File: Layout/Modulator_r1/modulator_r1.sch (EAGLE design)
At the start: 3 parts, among them IC1 FT232RL, U1 ATMEGA328P-AU

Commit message: Progress on board.
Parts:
- added C1: 10nF, resistor:C-EUC0603
- added C2: 100nF, resistor:C-EUC0603
- added C3: 4u7, resistor:C-EUC0603
- added J$2: SMA_EDGE, SparkFun-Connectors:SMA_EDGE
- added JP1: AVR_SPI_PRG_6NS, SparkFun-Connectors:AVR_SPI_PRG_6NS
- added JP2: USB-B, SparkFun-Connectors:USBPTH
- added L1: FB, resistor:L-EU0207/12
- added LED1, LED2, LED3, LED4: (no value), led:LEDCHIPLED_1206
- added U$1: CC1125RHBT, Texas Instruments_By_element14_Batch_1:CC1125RHBT
- added U$6: MCP1700T-3302E/TT, Ava:MCP1700T-3302E/TT
- added U2: TPS79933QDDCRQ1, Texas Instruments_By_element14_Batch_1:TPS79933QDDCRQ1
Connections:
- new net +3V3: JP1.2, U$6.VOUT, U1.AVCC, U1.VCC, U1.VCC_2
- new net AVR_NRESET: JP1.5, U1.PC6
- new net GND: C1.2, C2.2, C3.2, IC1.GND, IC1.GND@1, IC1.GND@2, IC1.GND@A, J$1.GND@0, J$1.GND@1, J$1.GND@2, J$1.GND@3, J$2.GND@0, J$2.GND@1, J$2.GND@2, J$2.GND@3, JP1.6, L1.2, LED1.C, LED2.C, LED3.C, LED4.C, U$1.GND_PAD, U$6.GND, U1.GND, U1.GND_2, U1.GND_3, U2.GND
- new net MISO: JP1.1, U$1.MISO, U1.PB4
- new net MOSI: JP1.4, U$1.MOSI, U1.PB3
- new net N$1: IC1.USBDM, JP2.D-
- new net N$2: IC1.USBDP, JP2.D+
- new net N$3: JP2.GND, L1.1
- new net NSS: U$1.CSN, U1.PB2
- new net SCK: JP1.3, U$1.SCK, U1.PB5
- new net UART_RX: IC1.RXD, U1.PD1
- new net UART_TX: IC1.TXD, U1.PD0
- new net VCCIO: C1.1, C2.1, C3.1, IC1.VCC, IC1.VCCIO, JP2.VBUS, U$6.VIN, U2.IN

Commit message: Layout progress.
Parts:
- added C10: 1n8, resistor:C-EUC0402
- added C11, C12: 12p, resistor:C-EUC0402
- added C13, C14, C18: 5p1, resistor:C-EUC0402
- added C15: 56p, resistor:C-EUC0402
- added C16: 39p, resistor:C-EUC0402
- added C17: 2p2, resistor:C-EUC0402
- added C19: 6p2, resistor:C-EUC0402
- added C20, C21, C22, C23, C24, C25, C26, C28, C29, C8, C9: 47n, resistor:C-EUC0402
- added C27: 100p, resistor:C-EUC0402
- added C4: 100nF, resistor:C-EUC0603
- added C5: 10nF, resistor:C-EUC0603
- added C6: 220n, resistor:C-EUC0402
- added C7: 10n, resistor:C-EUC0402
- added L2: FB, resistor:L-EU0207/10
- added L3, L6: 56n, resistor:L-EUL0402
- added L4, L5: 27n, resistor:L-EUL0402
- added L7: 15n, resistor:L-EUL0402
- added L8: 43n, resistor:L-EUL0402
- added L9: 22n, resistor:L-EUL0402
- added Q1: FA-20H, crystal:FA-20H
- added R1: 56K, resistor:R-EU_R0402
- added R2: 18R, resistor:R-EU_R0402
- L1: device resistor:L-EU0207/12 -> resistor:L-EU0207/10
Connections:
- new net CC_IO0: U$1.GPIO0
- new net CC_IO2: U$1.GPIO2
- new net CC_IO3: U$1.GPIO3
- new net CC_LNA_N: C13.2, L3.1, L4.1, U$1.LNA_N
- new net CC_LNA_P: C14.1, L3.2, L5.1, U$1.LNA_P
- new net CC_NRESET: U$1.NRESET
- new net CC_RF_PA: C16.2, L6.2, U$1.PA
- new net CC_VDD: C15.1, C20.1, C21.1, C22.1, C23.1, C24.1, C25.1, C26.1, C27.1, C28.1, C29.1, R2.2, U$1.AVDD_IF, U$1.AVDD_PFD_CHP, U$1.AVDD_RF, U$1.AVDD_SYNTH2, U$1.AVDD_SYNTH_1, U$1.AVDD_XOSC, U$1.DVDD_1, U$1.DVDD_2, U$1.VDD_GUARD, U2.OUT
- new net N$10: C7.1, U$1.DCPL_VCO
- new net N$11: C6.1, U$1.DCPL
- new net N$12: C10.2, U$1.LPF1
- new net N$13: C10.1, U$1.LPF0
- new net N$14: C11.1, Q1.1, U$1.XOSC_Q2
- new net N$15: C19.1, L8.1, L9.2
- new net N$16: C12.1, Q1.3, U$1.XOSC_Q1
- new net N$17: C14.2, J$1.SIGNAL, L4.2
- new net N$18: C17.1, C18.1, L7.1, L8.2
- new net N$19: C16.1, C17.2, L7.2
- new net N$21: C15.2, L6.1, R2.1
- new net N$4: C5.1, JP2.VBUS, L2.1
- new net N$5: C4.1, IC1.3V3OUT
- new net N$6: J$2.SIGNAL, L9.1
- new net N$7: R1.1, U$1.RBIAS
- new net N$8: C9.1, U$1.DCPL_XOSC
- new net N$9: C8.1, U$1.DCPL_PFD_CHIP
- net GND: now also C11.2, C12.2, C13.1, C18.2, C19.2, C20.2, C21.2, C22.2, C23.2, C24.2, C25.2, C26.2, C27.2, C28.2, C29.2, C4.2, C5.2, C6.2, C7.2, C8.2, C9.2, IC1.TEST, L5.2, Q1.2, Q1.4, R1.2
- net VCCIO: now also L2.2; no longer JP2.VBUS
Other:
- moved on the sheet: JP2, L1

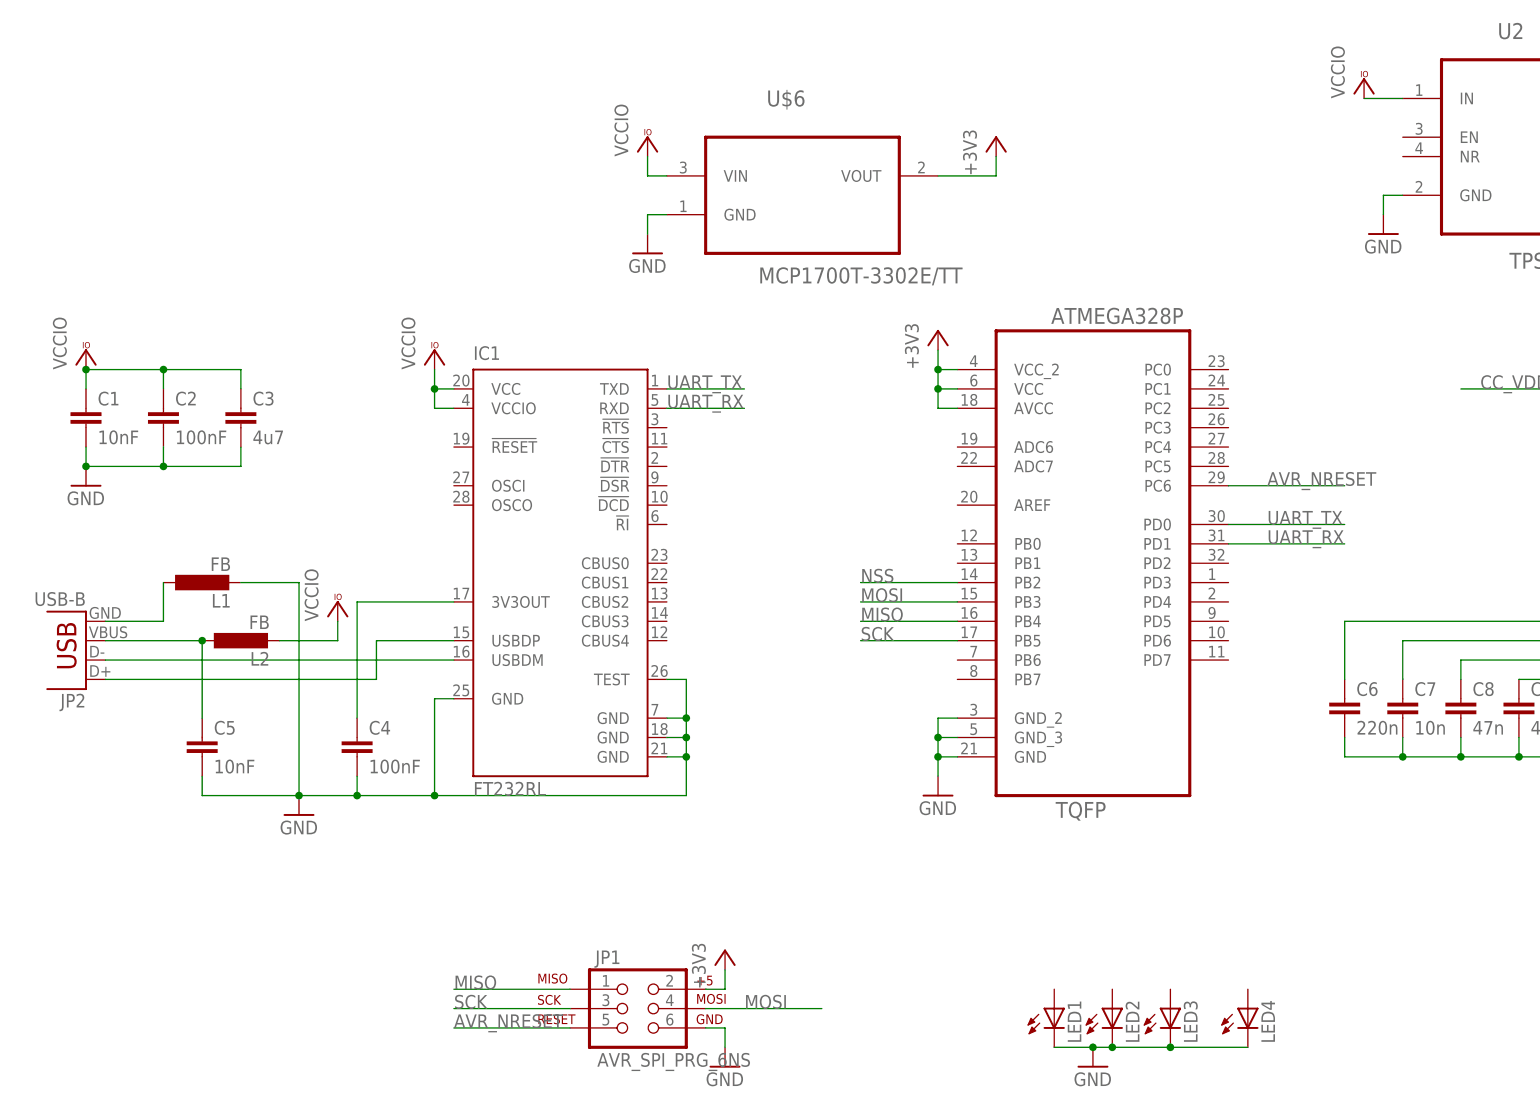
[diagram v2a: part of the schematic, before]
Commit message: Add USB power switch, start routing.
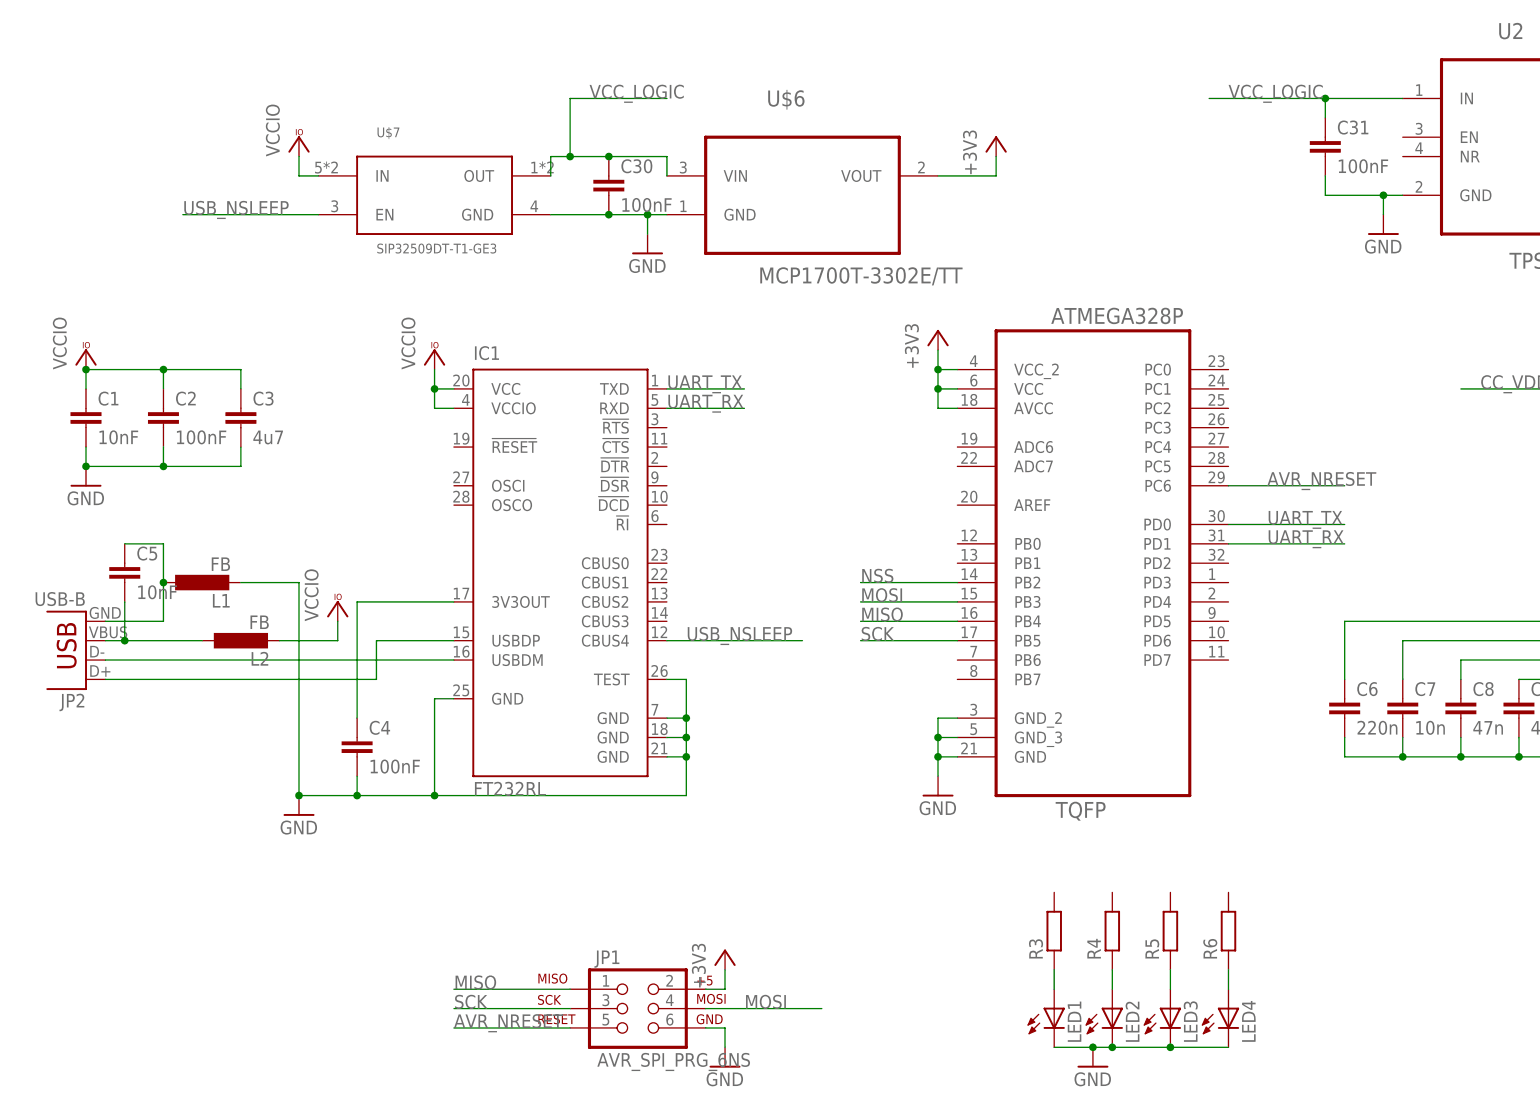
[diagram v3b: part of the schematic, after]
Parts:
- added C30, C31: 100nF, resistor:C-EUC0603
- added R3, R4, R5, R6: (no value), resistor:R-EU_R0603
- added U$7: SIP32509DT-T1-GE3, phil-ic:SIP32509DT-T1-GE3
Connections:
- new net N$22: LED1.A, R3.1
- new net N$23: LED2.A, R4.1
- new net N$24: LED3.A, R5.1
- new net N$25: LED4.A, R6.1
- new net USB_NSLEEP: IC1.CBUS4, U$7.EN
- new net VCC_LOGIC: C30.1, C31.1, U$6.VIN, U$7.OUT, U2.IN
- net GND: now also C30.2, C31.2, U$7.GND; no longer C5.2
- net N$3: now also C5.1
- net N$4: now also C5.2; no longer C5.1
- net VCCIO: now also U$7.IN; no longer U$6.VIN, U2.IN
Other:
- moved on the sheet: C5, LED4
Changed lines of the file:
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@@
 <part name="C2" library="resistor" deviceset="C-EU" device="C0603" value="100nF"/>
 <part name="C3" library="resistor" deviceset="C-EU" device="C0603" value="4u7"/>
-<part name="VCC3" library="supply1" deviceset="VCCIO" device=""/>
 <part name="GND5" library="supply1" deviceset="GND" device=""/>
 <part name="GND6" library="supply1" deviceset="GND" device=""/>
-<part name="VCC4" library="supply1" deviceset="VCCIO" device=""/>
 <part name="GND7" library="supply1" deviceset="GND" device=""/>
 <part name="+3V1" library="supply1" deviceset="+3V3" device=""/>
@@
 <part name="C28" library="resistor" deviceset="C-EU" device="C0402" value="47n"/>
 <part name="C29" library="resistor" deviceset="C-EU" device="C0402" value="47n"/>
+<part name="U$7" library="phil-ic" deviceset="SIP32509DT-T1-GE3" device=""/>
+<part name="VCC6" library="supply1" deviceset="VCCIO" device=""/>
+<part name="C30" library="resistor" deviceset="C-EU" device="C0603" value="100nF"/>
+<part name="R3" library="resistor" deviceset="R-EU_" device="R0603"/>
+<part name="R4" library="resistor" deviceset="R-EU_" device="R0603"/>
+<part name="R5" library="resistor" deviceset="R-EU_" device="R0603"/>
+<part name="R6" library="resistor" deviceset="R-EU_" device="R0603"/>
+<part name="C31" library="resistor" deviceset="C-EU" device="C0603" value="100nF"/>
 </parts>
 <sheets>
@@
 <instance part="LED2" gate="G$1" x="45.72" y="-22.86"/>
 <instance part="LED3" gate="G$1" x="53.34" y="-22.86"/>
-<instance part="LED4" gate="G$1" x="63.5" y="-22.86"/>
+<instance part="LED4" gate="G$1" x="60.96" y="-22.86"/>
 <instance part="U$6" gate="A" x="5.08" y="86.36"/>
 <instance part="L1" gate="G$1" x="-73.66" y="33.02" rot="R90"/>
@@
 <instance part="C2" gate="G$1" x="-78.74" y="55.88"/>
 <instance part="C3" gate="G$1" x="-68.58" y="55.88"/>
-<instance part="VCC3" gate="G$1" x="-15.24" y="91.44"/>
 <instance part="GND5" gate="1" x="-15.24" y="76.2"/>
 <instance part="GND6" gate="1" x="81.28" y="78.74"/>
-<instance part="VCC4" gate="G$1" x="78.74" y="99.06"/>
 <instance part="GND7" gate="1" x="-5.08" y="-30.48"/>
 <instance part="+3V1" gate="G$1" x="30.48" y="91.44"/>
@@
 <instance part="C4" gate="G$1" x="-53.34" y="12.7"/>
 <instance part="L2" gate="G$1" x="-68.58" y="25.4" rot="R90"/>
-<instance part="C5" gate="G$1" x="-73.66" y="12.7"/>
+<instance part="C5" gate="G$1" x="-83.82" y="35.56"/>
 <instance part="C6" gate="G$1" x="76.2" y="17.78"/>
 <instance part="C7" gate="G$1" x="83.82" y="17.78"/>
@@
 <instance part="C28" gate="G$1" x="175.26" y="93.98"/>
 <instance part="C29" gate="G$1" x="182.88" y="93.98"/>
+<instance part="U$7" gate="G$1" x="-43.18" y="83.82"/>
+<instance part="VCC6" gate="G$1" x="-60.96" y="91.44"/>
+<instance part="C30" gate="G$1" x="-20.32" y="86.36"/>
+<instance part="R3" gate="G$1" x="38.1" y="-12.7" rot="R90"/>
+<instance part="R4" gate="G$1" x="45.72" y="-12.7" rot="R90"/>
+<instance part="R5" gate="G$1" x="53.34" y="-12.7" rot="R90"/>
+<instance part="R6" gate="G$1" x="60.96" y="-12.7" rot="R90"/>
+<instance part="C31" gate="G$1" x="73.66" y="91.44"/>
 </instances>
 <busses>
@@
 <wire x1="-53.34" y1="7.62" x2="-53.34" y2="5.08" width="0.1524" layer="91"/>
 <junction x="-53.34" y="5.08"/>
-<pinref part="C5" gate="G$1" pin="2"/>
-<wire x1="-73.66" y1="7.62" x2="-73.66" y2="5.08" width="0.1524" layer="91"/>
-<wire x1="-73.66" y1="5.08" x2="-60.96" y2="5.08" width="0.1524" layer="91"/>
 </segment>
 <segment>
@@
 <pinref part="U$6" gate="A" pin="GND"/>
 <wire x1="-15.24" y1="81.28" x2="-12.7" y2="81.28" width="0.1524" layer="91"/>
+<pinref part="U$7" gate="G$1" pin="GND"/>
+<wire x1="-15.24" y1="81.28" x2="-20.32" y2="81.28" width="0.1524" layer="91"/>
+<junction x="-15.24" y="81.28"/>
+<pinref part="C30" gate="G$1" pin="2"/>
+<wire x1="-20.32" y1="81.28" x2="-27.94" y2="81.28" width="0.1524" layer="91"/>
+<junction x="-20.32" y="81.28"/>
 </segment>
 <segment>
@@
 <pinref part="U2" gate="A" pin="GND"/>
 <wire x1="81.28" y1="83.82" x2="83.82" y2="83.82" width="0.1524" layer="91"/>
+<pinref part="C31" gate="G$1" pin="2"/>
+<wire x1="81.28" y1="83.82" x2="73.66" y2="83.82" width="0.1524" layer="91"/>
+<wire x1="73.66" y1="83.82" x2="73.66" y2="86.36" width="0.1524" layer="91"/>
+<junction x="81.28" y="83.82"/>
 </segment>
 <segment>
@@
 <junction x="45.72" y="-27.94"/>
 <pinref part="LED4" gate="G$1" pin="C"/>
-<wire x1="53.34" y1="-27.94" x2="63.5" y2="-27.94" width="0.1524" layer="91"/>
+<wire x1="53.34" y1="-27.94" x2="60.96" y2="-27.94" width="0.1524" layer="91"/>
 <junction x="53.34" y="-27.94"/>
 <pinref part="GND8" gate="1" pin="GND"/>
@@
 <wire x1="-86.36" y1="27.94" x2="-78.74" y2="27.94" width="0.1524" layer="91"/>
 <wire x1="-78.74" y1="27.94" x2="-78.74" y2="33.02" width="0.1524" layer="91"/>
+<wire x1="-78.74" y1="33.02" x2="-78.74" y2="38.1" width="0.1524" layer="91"/>
+<junction x="-78.74" y="33.02"/>
+<pinref part="C5" gate="G$1" pin="1"/>
+<wire x1="-78.74" y1="38.1" x2="-83.82" y2="38.1" width="0.1524" layer="91"/>
 </segment>
 </net>
@@
 </segment>
 <segment>
-<pinref part="U$6" gate="A" pin="VIN"/>
-<pinref part="VCC3" gate="G$1" pin="VCCIO"/>
-<wire x1="-12.7" y1="86.36" x2="-15.24" y2="86.36" width="0.1524" layer="91"/>
-<wire x1="-15.24" y1="86.36" x2="-15.24" y2="88.9" width="0.1524" layer="91"/>
-</segment>
-<segment>
-<pinref part="VCC4" gate="G$1" pin="VCCIO"/>
-<pinref part="U2" gate="A" pin="IN"/>
-<wire x1="78.74" y1="96.52" x2="83.82" y2="96.52" width="0.1524" layer="91"/>
-</segment>
-<segment>
 <pinref part="IC1" gate="1" pin="VCCIO"/>
 <wire x1="-40.64" y1="55.88" x2="-43.18" y2="55.88" width="0.1524" layer="91"/>
@@
 <wire x1="-40.64" y1="58.42" x2="-43.18" y2="58.42" width="0.1524" layer="91"/>
 <junction x="-43.18" y="58.42"/>
+</segment>
+<segment>
+<pinref part="U$7" gate="G$1" pin="IN"/>
+<pinref part="VCC6" gate="G$1" pin="VCCIO"/>
+<wire x1="-58.42" y1="86.36" x2="-60.96" y2="86.36" width="0.1524" layer="91"/>
+<wire x1="-60.96" y1="86.36" x2="-60.96" y2="88.9" width="0.1524" layer="91"/>
 </segment>
 </net>
@@
 <pinref part="JP2" gate="G$1" pin="VBUS"/>
 <pinref part="L2" gate="G$1" pin="1"/>
-<wire x1="-86.36" y1="25.4" x2="-73.66" y2="25.4" width="0.1524" layer="91"/>
-<pinref part="C5" gate="G$1" pin="1"/>
-<wire x1="-73.66" y1="15.24" x2="-73.66" y2="25.4" width="0.1524" layer="91"/>
-<junction x="-73.66" y="25.4"/>
+<wire x1="-86.36" y1="25.4" x2="-83.82" y2="25.4" width="0.1524" layer="91"/>
+<pinref part="C5" gate="G$1" pin="2"/>
+<wire x1="-83.82" y1="25.4" x2="-73.66" y2="25.4" width="0.1524" layer="91"/>
+<wire x1="-83.82" y1="30.48" x2="-83.82" y2="25.4" width="0.1524" layer="91"/>
+<junction x="-83.82" y="25.4"/>
 </segment>
 </net>
@@
 </segment>
 </net>
+<net name="USB_NSLEEP" class="0">
+<segment>
+<pinref part="IC1" gate="1" pin="CBUS4"/>
+<wire x1="-12.7" y1="25.4" x2="5.08" y2="25.4" width="0.1524" layer="91"/>
+<label x="-10.16" y="25.4" size="1.778" layer="95"/>
+</segment>
+<segment>
+<pinref part="U$7" gate="G$1" pin="EN"/>
+<wire x1="-58.42" y1="81.28" x2="-76.2" y2="81.28" width="0.1524" layer="91"/>
+<label x="-76.2" y="81.28" size="1.778" layer="95"/>
+</segment>
+</net>
+<net name="VCC_LOGIC" class="0">
+<segment>
+<pinref part="U$6" gate="A" pin="VIN"/>
+<wire x1="-12.7" y1="86.36" x2="-12.7" y2="88.9" width="0.1524" layer="91"/>
+<pinref part="C30" gate="G$1" pin="1"/>
+<wire x1="-12.7" y1="88.9" x2="-20.32" y2="88.9" width="0.1524" layer="91"/>
+<pinref part="U$7" gate="G$1" pin="OUT"/>
+<wire x1="-20.32" y1="88.9" x2="-25.4" y2="88.9" width="0.1524" layer="91"/>
+<wire x1="-25.4" y1="88.9" x2="-27.94" y2="88.9" width="0.1524" layer="91"/>
+<wire x1="-27.94" y1="88.9" x2="-27.94" y2="86.36" width="0.1524" layer="91"/>
+<junction x="-20.32" y="88.9"/>
+<wire x1="-25.4" y1="88.9" x2="-25.4" y2="96.52" width="0.1524" layer="91"/>
+<junction x="-25.4" y="88.9"/>
+<wire x1="-25.4" y1="96.52" x2="-12.7" y2="96.52" width="0.1524" layer="91"/>
+<label x="-22.86" y="96.52" size="1.778" layer="95"/>
+</segment>
+<segment>
+<pinref part="U2" gate="A" pin="IN"/>
+<wire x1="58.42" y1="96.52" x2="73.66" y2="96.52" width="0.1524" layer="91"/>
+<label x="60.96" y="96.52" size="1.778" layer="95"/>
+<pinref part="C31" gate="G$1" pin="1"/>
+<wire x1="73.66" y1="96.52" x2="83.82" y2="96.52" width="0.1524" layer="91"/>
+<wire x1="73.66" y1="93.98" x2="73.66" y2="96.52" width="0.1524" layer="91"/>
+<junction x="73.66" y="96.52"/>
+</segment>
+</net>
+<net name="N$22" class="0">
+<segment>
+<pinref part="R3" gate="G$1" pin="1"/>
+<pinref part="LED1" gate="G$1" pin="A"/>
+<wire x1="38.1" y1="-17.78" x2="38.1" y2="-20.32" width="0.1524" layer="91"/>
+</segment>
+</net>
+<net name="N$23" class="0">
+<segment>
+<pinref part="R4" gate="G$1" pin="1"/>
+<pinref part="LED2" gate="G$1" pin="A"/>
+<wire x1="45.72" y1="-17.78" x2="45.72" y2="-20.32" width="0.1524" layer="91"/>
+</segment>
+</net>
+<net name="N$24" class="0">
+<segment>
+<pinref part="R5" gate="G$1" pin="1"/>
+<pinref part="LED3" gate="G$1" pin="A"/>
+<wire x1="53.34" y1="-17.78" x2="53.34" y2="-20.32" width="0.1524" layer="91"/>
+</segment>
+</net>
+<net name="N$25" class="0">
+<segment>
+<pinref part="R6" gate="G$1" pin="1"/>
+<pinref part="LED4" gate="G$1" pin="A"/>
+<wire x1="60.96" y1="-17.78" x2="60.96" y2="-20.32" width="0.1524" layer="91"/>
+</segment>
+</net>

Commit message: Add switches, general layout churn.
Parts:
- added C32, C33: 100nF, resistor:C-EUC0603
- added R10, R7, R8, R9: (no value), resistor:R-EU_R0603
- added S1, S2, S3, S4, S5: SWITCH-MOMENTARY-2PTH, SparkFun-Electromechanical:SWITCH-MOMENTARY-2PTH
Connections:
- new net AVR_L1: R3.2, U1.PC0
- new net AVR_L2: R4.2, U1.PC1
- new net AVR_L3: R5.2, U1.PC2
- new net AVR_L4: R6.2, U1.PC3
- new net AVR_S1: R7.2, S1.1, U1.PD2
- new net AVR_S2: R8.2, S2.1, U1.PD3
- new net AVR_S3: R9.2, S3.1, U1.PD4
- new net AVR_S4: R10.2, S4.1, U1.PD5
- net +3V3: now also C32.1, C33.1, S1.2, S2.2, S3.2, S4.2
- net AVR_NRESET: now also S5.2
- net GND: now also C32.2, C33.2, R10.1, R7.1, R8.1, R9.1, S5.1

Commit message: Progress.
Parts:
- removed L1, L2: FB, resistor:L-EU0207/10
- added FB1, FB2: (no value), resistor:R-EU_R0603
- renumbered IC1 to U5, U$1 to U3, U$6 to U4, U$7 to U6
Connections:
- net GND: now also FB1.2; no longer L1.2
- net N$3: now also FB1.1; no longer L1.1
- net N$4: now also FB2.1; no longer L2.1
- net VCCIO: now also FB2.2; no longer L2.2
